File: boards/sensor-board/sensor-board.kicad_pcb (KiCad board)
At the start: 2 copper layers, 41.1 x 32 mm, 21 parts, among them J1 Conn_01x02, J2 Conn_01x03, J3 Conn_01x02, U1 NE5532

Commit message: general changes
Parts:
- removed J2: Conn_01x03, Connector_PinHeader_2.54mm:PinHeader_1x03_P2.54mm_Vertical
- removed REF** (x2): Hole-2.4mm-NPTH, oresat-misc:Hole-2.4mm-NPTH
- added J4: Conn_01x04, Connector_JST:JST_EH_B4B-EH-A_1x04_P2.50mm_Vertical, F.Cu at (138.3, 60.8)
- C2: value 1u -> NP
- R2: value 10k -> NP
- R3: value 1k -> 0
- moved TP4 1.50 mm to (134.4, 63.3)
- moved TP6 1.50 mm to (134.4, 60.7)
- moved TP5 1.20 mm to (134.7, 65.9)

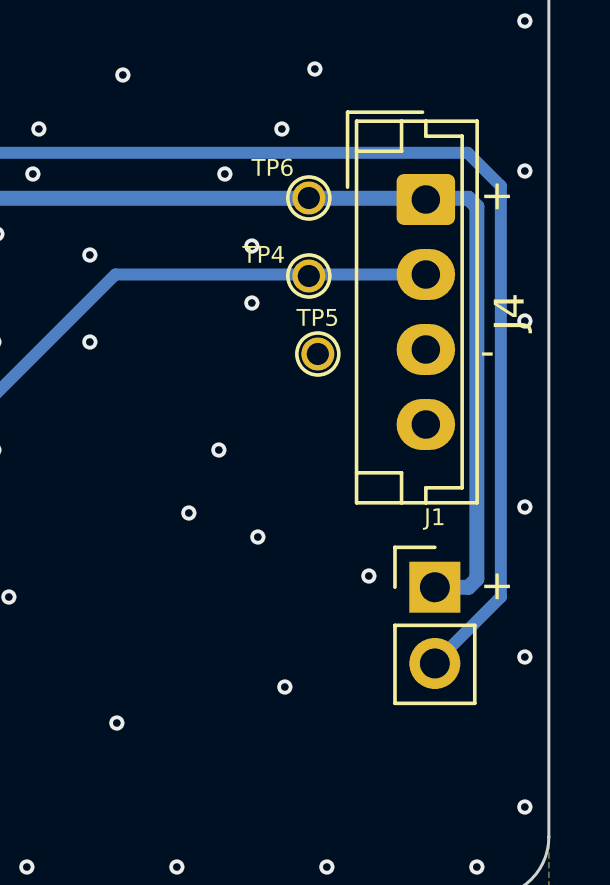
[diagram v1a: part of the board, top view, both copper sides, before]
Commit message: condensed 3-pin and 2-pin connectors to controller board into one 4-pin connector
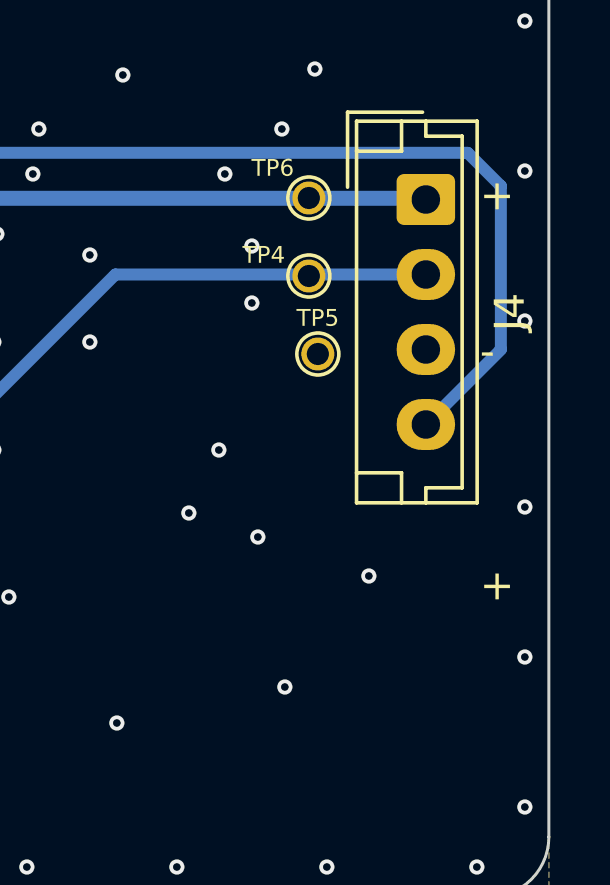
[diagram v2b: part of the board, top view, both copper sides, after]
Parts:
- removed J1: Conn_01x02, Connector_PinHeader_2.54mm:PinHeader_1x02_P2.54mm_Vertical
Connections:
- J3 pad 2: Net-(J1-Pin_2) -> Net-(J3-Pin_2)
- J4 pad 4: unconnected-(J4-Pin_4-Pad4) -> Net-(J3-Pin_2)
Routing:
- net Net-(J1-Pin_2): track 53.6 -> 0.00 mm
- net Net-(J3-Pin_2): track 0.00 -> 45.8 mm
- net +3.3V: track 64.9 -> 49.4 mm
